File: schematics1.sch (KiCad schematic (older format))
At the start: 14 parts, among them J1 Keypad, SW1 SW_SPST, U1 EA_T123X-I2C

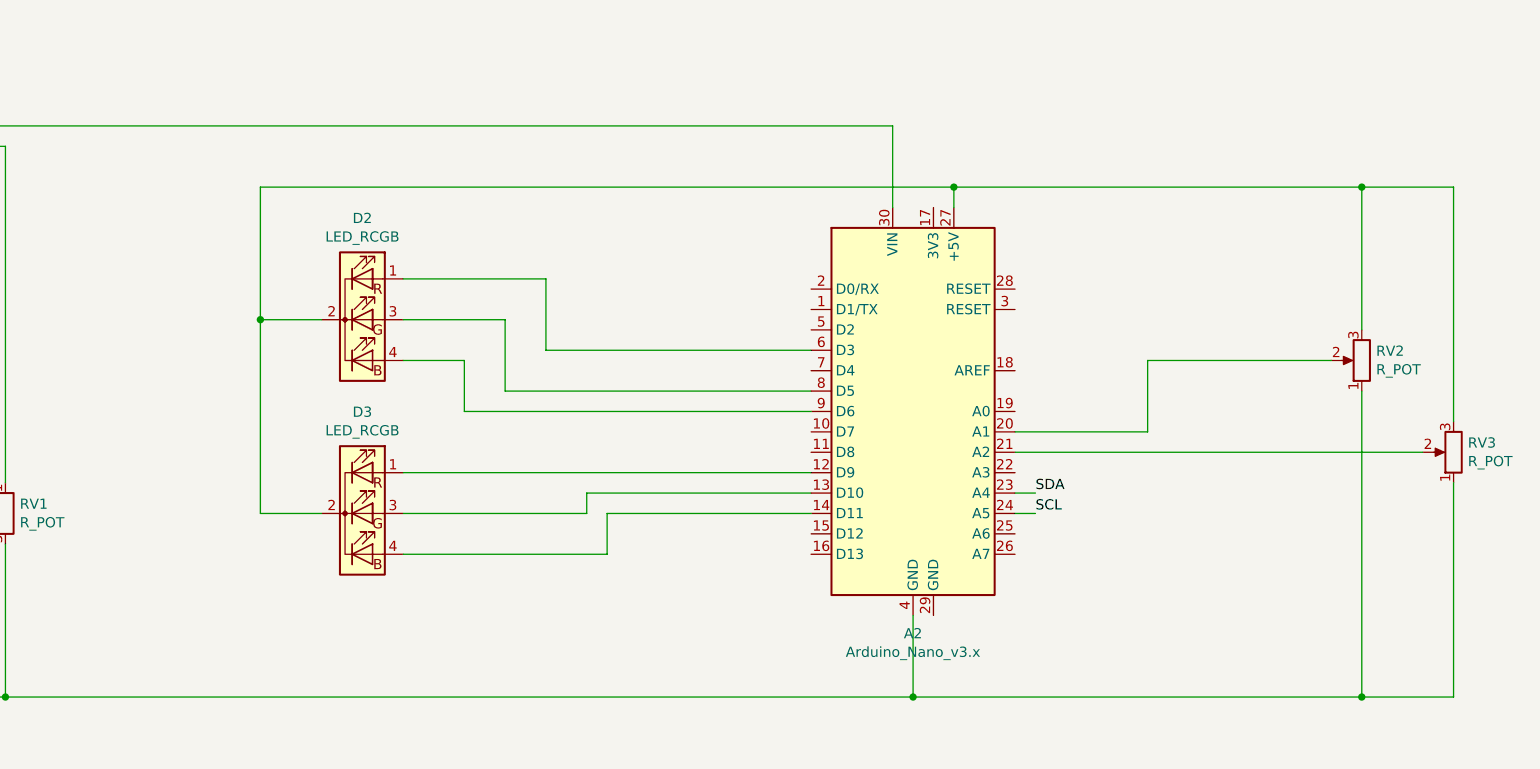
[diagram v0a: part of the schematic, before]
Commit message: Removed RGB, added switches and charlieplex leds to Nano2
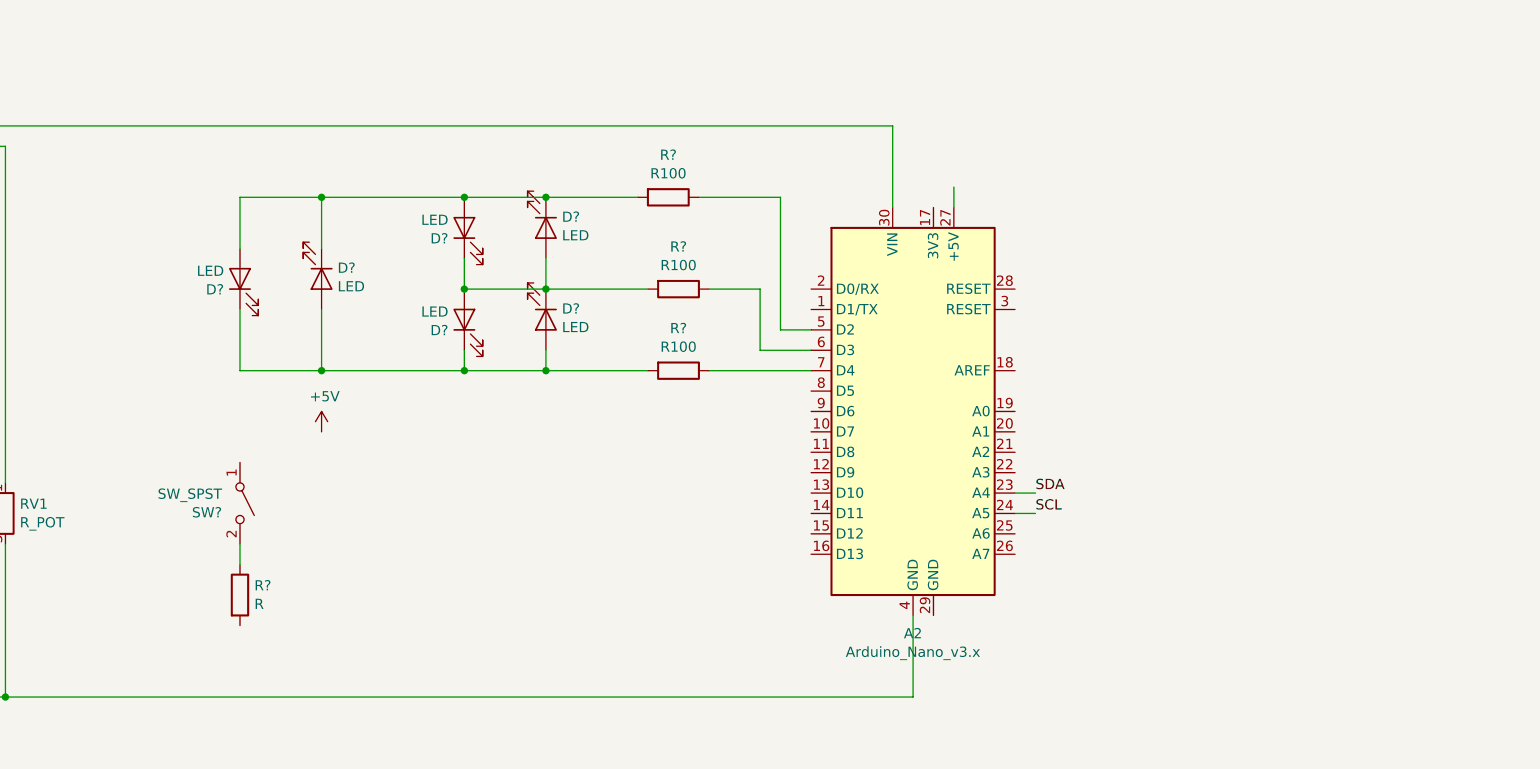
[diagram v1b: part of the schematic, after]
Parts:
- removed D2, D3: LED_RCGB, symbol Device:LED_RCGB
- removed RV2, RV3: R_POT, symbol Device:R_POT
- added D? (x6): LED, symbol Device:LED
- added R? (x3): R100, symbol Device:R
- added R?: R, symbol Device:R
- added SW?: SW_SPST, symbol Switch:SW_SPST
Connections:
- net labels added: +5V
- wire segments 93 -> 86
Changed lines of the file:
@@
 Text Label 5600 4700 0    50   ~ 0
 SDA
-$Comp
-L MCU_Module:Arduino_Nano_v3.x A2
-U 1 1 5D9BED68
-P 11600 4400
-F 0 "A2" H 11600 3311 50  0000 C CNN
-F 1 "Arduino_Nano_v3.x" H 11600 3220 50  0000 C CNN
-F 2 "Module:Arduino_Nano" H 11750 3450 50  0001 L CNN
-F 3 "http://www.mouser.com/pdfdocs/Gravitech_Arduino_Nano3_0.pdf" H 11600 3400 50  0001 C CNN
-	1    11600 4400
-	1    0    0    -1
-$EndComp
 Wire Wire Line
 	4900 3000 4900 3300
@@
 	3950 5800 5000 5800
 Connection ~ 5000 5800
-$Comp
-L Device:LED_RCGB D2
-U 1 1 5D9FD82A
-P 8900 3950
-F 0 "D2" H 8900 4447 50  0000 C CNN
-F 1 "LED_RCGB" H 8900 4356 50  0000 C CNN
-F 2 "" H 8900 3900 50  0001 C CNN
-F 3 "~" H 8900 3900 50  0001 C CNN
-	1    8900 3950
-	1    0    0    -1
-$EndComp
-$Comp
-L Device:LED_RCGB D3
-U 1 1 5D9FEB80
-P 8900 4900
-F 0 "D3" H 8900 5397 50  0000 C CNN
-F 1 "LED_RCGB" H 8900 5306 50  0000 C CNN
-F 2 "" H 8900 4850 50  0001 C CNN
-F 3 "~" H 8900 4850 50  0001 C CNN
-	1    8900 4900
-	1    0    0    -1
-$EndComp
-Wire Wire Line
-	9100 3750 9800 3750
-Wire Wire Line
-	9800 3750 9800 4100
-Wire Wire Line
-	9800 4100 11100 4100
-Wire Wire Line
-	9100 3950 9600 3950
-Wire Wire Line
-	9600 3950 9600 4300
-Wire Wire Line
-	9600 4300 11100 4300
-Wire Wire Line
-	9100 4150 9400 4150
-Wire Wire Line
-	9400 4150 9400 4400
-Wire Wire Line
-	9400 4400 11100 4400
-Wire Wire Line
-	11100 4700 9100 4700
-Wire Wire Line
-	9100 4900 10000 4900
-Wire Wire Line
-	10000 4900 10000 4800
-Wire Wire Line
-	10000 4800 11100 4800
-Wire Wire Line
-	11100 4900 10100 4900
-Wire Wire Line
-	10100 4900 10100 5100
-Wire Wire Line
-	10100 5100 9100 5100
 Wire Wire Line
 	6450 3000 11500 3000
@@
 Wire Wire Line
 	11800 3400 11800 3300
-Wire Wire Line
-	11800 3300 8400 3300
-Wire Wire Line
-	8400 3300 8400 3950
-Wire Wire Line
-	8400 4900 8700 4900
-Wire Wire Line
-	8700 3950 8400 3950
-Connection ~ 8400 3950
-Wire Wire Line
-	8400 3950 8400 4900
-$Comp
-L Device:R_POT RV2
-U 1 1 5DA10FB2
-P 13800 4150
-F 0 "RV2" H 13730 4104 50  0000 R CNN
-F 1 "R_POT" H 13730 4195 50  0000 R CNN
-F 2 "" H 13800 4150 50  0001 C CNN
-F 3 "~" H 13800 4150 50  0001 C CNN
-	1    13800 4150
-	-1   0    0    1
-$EndComp
-$Comp
-L Device:R_POT RV3
-U 1 1 5DA12230
-P 14250 4600
-F 0 "RV3" H 14180 4554 50  0000 R CNN
-F 1 "R_POT" H 14180 4645 50  0000 R CNN
-F 2 "" H 14250 4600 50  0001 C CNN
-F 3 "~" H 14250 4600 50  0001 C CNN
-	1    14250 4600
-	-1   0    0    1
-$EndComp
-Wire Wire Line
-	13650 4150 12750 4150
-Wire Wire Line
-	12750 4150 12750 4500
-Wire Wire Line
-	12750 4500 12100 4500
-Wire Wire Line
-	12100 4600 14100 4600
-Wire Wire Line
-	14250 4450 14250 3300
-Wire Wire Line
-	14250 3300 13800 3300
-Connection ~ 11800 3300
-Wire Wire Line
-	13800 4000 13800 3300
-Connection ~ 13800 3300
-Wire Wire Line
-	13800 3300 11800 3300
-Wire Wire Line
-	11600 5800 13800 5800
-Wire Wire Line
-	14250 5800 14250 4750
-Connection ~ 11600 5800
-Wire Wire Line
-	13800 4300 13800 5800
-Connection ~ 13800 5800
-Wire Wire Line
-	13800 5800 14250 5800
+$Comp
+L Device:LED D?
+U 1 1 5DAAD0C9
+P 8300 3750
+F 0 "D?" V 8247 3828 50  0000 L CNN
+F 1 "LED" V 8338 3828 50  0000 L CNN
+F 2 "" H 8300 3750 50  0001 C CNN
+F 3 "~" H 8300 3750 50  0001 C CNN
+	1    8300 3750
+	0    -1   -1   0
+$EndComp
+$Comp
+L Device:LED D?
+U 1 1 5DAAE2DF
+P 9400 3950
+F 0 "D?" V 9347 4028 50  0000 L CNN
+F 1 "LED" V 9438 4028 50  0000 L CNN
+F 2 "" H 9400 3950 50  0001 C CNN
+F 3 "~" H 9400 3950 50  0001 C CNN
+	1    9400 3950
+	0    -1   -1   0
+$EndComp
+$Comp
+L Device:LED D?
+U 1 1 5DAAE59B
+P 9800 3500
+F 0 "D?" V 9747 3578 50  0000 L CNN
+F 1 "LED" V 9838 3578 50  0000 L CNN
+F 2 "" H 9800 3500 50  0001 C CNN
+F 3 "~" H 9800 3500 50  0001 C CNN
+	1    9800 3500
+	0    1    1    0
+$EndComp
+$Comp
+L Device:LED D?
+U 1 1 5DAAFB45
+P 9400 3500
+F 0 "D?" V 9347 3578 50  0000 L CNN
+F 1 "LED" V 9438 3578 50  0000 L CNN
+F 2 "" H 9400 3500 50  0001 C CNN
+F 3 "~" H 9400 3500 50  0001 C CNN
+	1    9400 3500
+	0    -1   -1   0
+$EndComp
+$Comp
+L Device:LED D?
+U 1 1 5DAAFEED
+P 9800 3950
+F 0 "D?" V 9747 4028 50  0000 L CNN
+F 1 "LED" V 9838 4028 50  0000 L CNN
+F 2 "" H 9800 3950 50  0001 C CNN
+F 3 "~" H 9800 3950 50  0001 C CNN
+	1    9800 3950
+	0    1    1    0
+$EndComp
+$Comp
+L Device:LED D?
+U 1 1 5DAB05F7
+P 8700 3750
+F 0 "D?" V 8647 3828 50  0000 L CNN
+F 1 "LED" V 8738 3828 50  0000 L CNN
+F 2 "" H 8700 3750 50  0001 C CNN
+F 3 "~" H 8700 3750 50  0001 C CNN
+	1    8700 3750
+	0    1    1    0
+$EndComp
+$Comp
+L MCU_Module:Arduino_Nano_v3.x A2
+U 1 1 5D9BED68
+P 11600 4400
+F 0 "A2" H 11600 3311 50  0000 C CNN
+F 1 "Arduino_Nano_v3.x" H 11600 3220 50  0000 C CNN
+F 2 "Module:Arduino_Nano" H 11750 3450 50  0001 L CNN
+F 3 "http://www.mouser.com/pdfdocs/Gravitech_Arduino_Nano3_0.pdf" H 11600 3400 50  0001 C CNN
+	1    11600 4400
+	1    0    0    -1
+$EndComp
+$Comp
+L Device:R R?
+U 1 1 5DAD04B2
+P 10400 3350
+F 0 "R?" V 10193 3350 50  0000 C CNN
+F 1 "R100" V 10284 3350 50  0000 C CNN
+F 2 "" V 10330 3350 50  0001 C CNN
+F 3 "~" H 10400 3350 50  0001 C CNN
+	1    10400 3350
+	0    1    1    0
+$EndComp
+$Comp
+L Device:R R?
+U 1 1 5DAD0C01
+P 10450 3800
+F 0 "R?" V 10243 3800 50  0000 C CNN
+F 1 "R100" V 10334 3800 50  0000 C CNN
+F 2 "" V 10380 3800 50  0001 C CNN
+F 3 "~" H 10450 3800 50  0001 C CNN
+	1    10450 3800
+	0    1    1    0
+$EndComp
+$Comp
+L Device:R R?
+U 1 1 5DAD0EB3
+P 10450 4200
+F 0 "R?" V 10243 4200 50  0000 C CNN
+F 1 "R100" V 10334 4200 50  0000 C CNN
+F 2 "" V 10380 4200 50  0001 C CNN
+F 3 "~" H 10450 4200 50  0001 C CNN
+	1    10450 4200
+	0    1    1    0
+$EndComp
+Wire Wire Line
+	11100 4000 10950 4000
+Wire Wire Line
+	10950 4000 10950 3350
+Wire Wire Line
+	10950 3350 10550 3350
+Wire Wire Line
+	10250 3350 9800 3350
+Wire Wire Line
+	9800 3350 9400 3350
+Wire Wire Line
+	8300 3350 8300 3600
+Connection ~ 9800 3350
+Connection ~ 9400 3350
+Wire Wire Line
+	9400 3350 8700 3350
+Wire Wire Line
+	8700 3600 8700 3350
+Connection ~ 8700 3350
+Wire Wire Line
+	8700 3350 8300 3350
+Wire Wire Line
+	11100 4100 10850 4100
+Wire Wire Line
+	10850 4100 10850 3800
+Wire Wire Line
+	10850 3800 10600 3800
+Wire Wire Line
+	10300 3800 9800 3800
+Wire Wire Line
+	9400 3800 9800 3800
+Connection ~ 9800 3800
+Wire Wire Line
+	9800 3650 9800 3800
+Wire Wire Line
+	9400 3650 9400 3800
+Connection ~ 9400 3800
+Wire Wire Line
+	11100 4200 10600 4200
+Wire Wire Line
+	10300 4200 9800 4200
+Wire Wire Line
+	8300 4200 8300 3900
+Wire Wire Line
+	8700 3900 8700 4200
+Connection ~ 8700 4200
+Wire Wire Line
+	8700 4200 8300 4200
+Wire Wire Line
+	9400 4100 9400 4200
+Connection ~ 9400 4200
+Wire Wire Line
+	9400 4200 8700 4200
+Wire Wire Line
+	9800 4100 9800 4200
+Connection ~ 9800 4200
+Wire Wire Line
+	9800 4200 9400 4200
+$Comp
+L Switch:SW_SPST SW?
+U 1 1 5DAE8628
+P 8300 4850
+F 0 "SW?" V 8346 4762 50  0000 R CNN
+F 1 "SW_SPST" V 8255 4762 50  0000 R CNN
+F 2 "" H 8300 4850 50  0001 C CNN
+F 3 "~" H 8300 4850 50  0001 C CNN
+	1    8300 4850
+	0    1    1    0
+$EndComp
+$Comp
+L Device:R R?
+U 1 1 5DAEDDF2
+P 8300 5300
+F 0 "R?" H 8370 5346 50  0000 L CNN
+F 1 "R" H 8370 5255 50  0000 L CNN
+F 2 "" V 8230 5300 50  0001 C CNN
+F 3 "~" H 8300 5300 50  0001 C CNN
+	1    8300 5300
+	1    0    0    -1
+$EndComp
+Wire Wire Line
+	8300 5050 8300 5150
+$Comp
+L power:+5V #PWR?
+U 1 1 5DAF87E0
+P 8700 4500
+F 0 "#PWR?" H 8700 4350 50  0001 C CNN
+F 1 "+5V" H 8715 4673 50  0000 C CNN
+F 2 "" H 8700 4500 50  0001 C CNN
+F 3 "" H 8700 4500 50  0001 C CNN
+	1    8700 4500
+	1    0    0    -1
+$EndComp
 $EndSCHEMATC

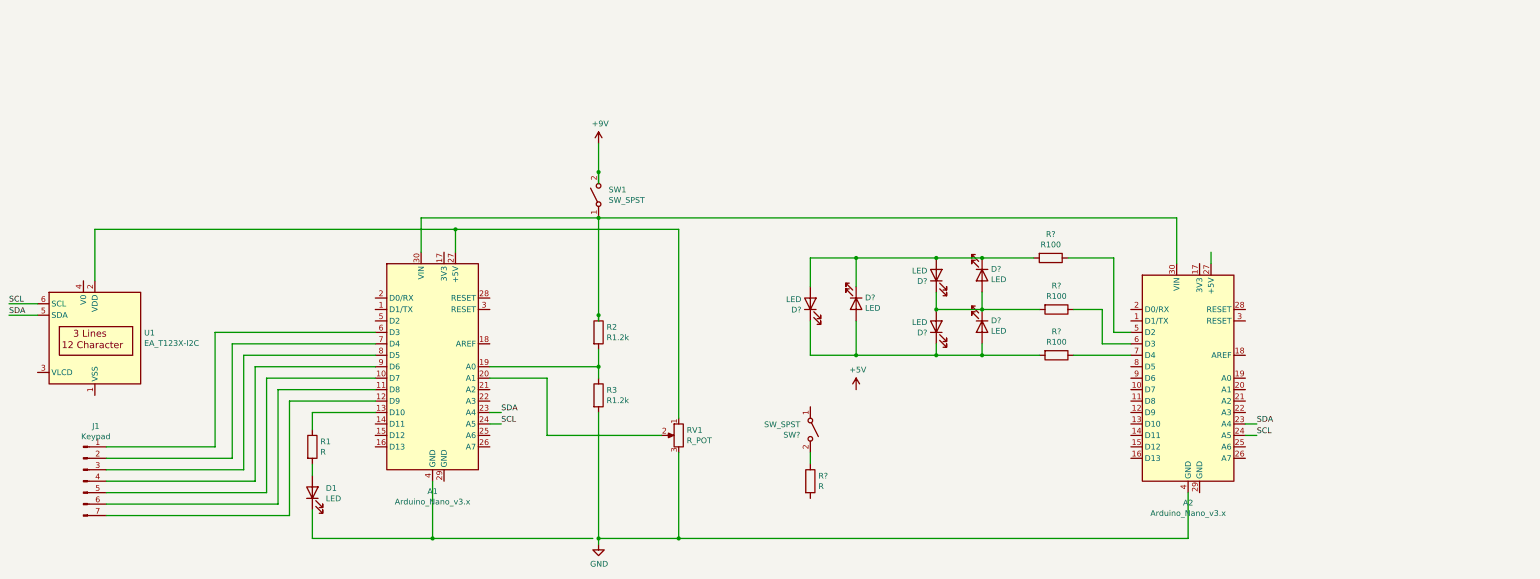
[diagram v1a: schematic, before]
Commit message: Added charlieplexed leds
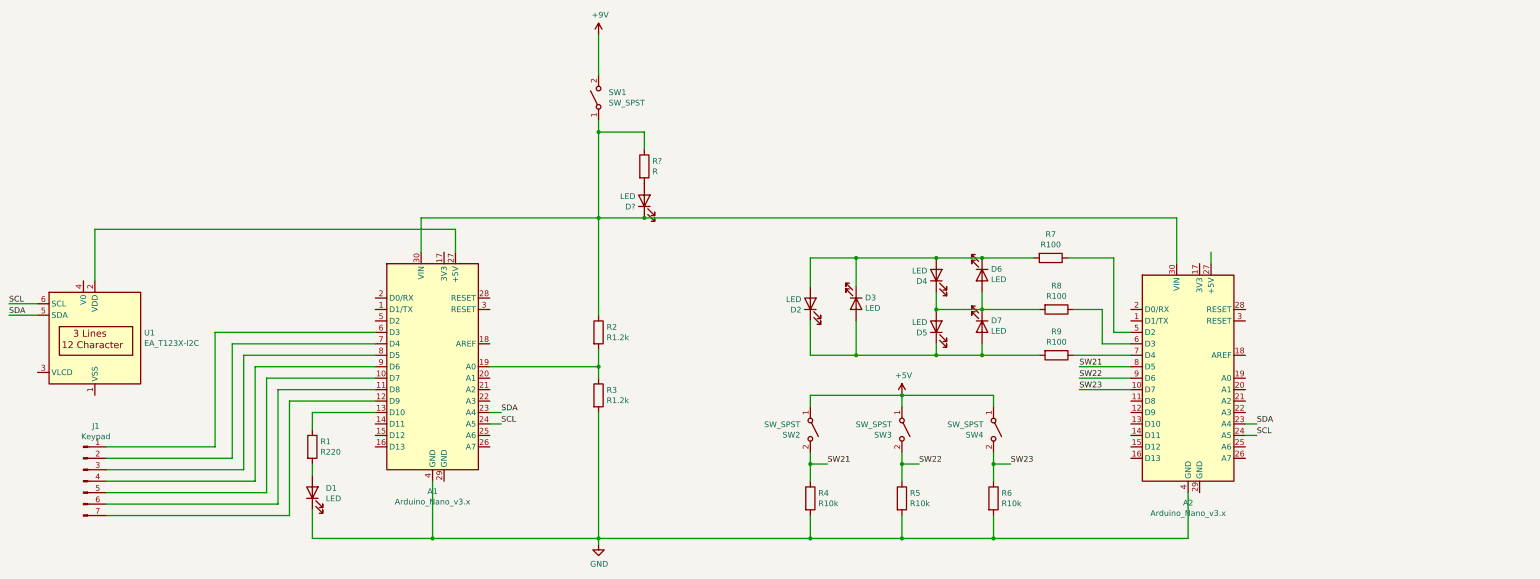
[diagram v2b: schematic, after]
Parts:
- removed RV1: R_POT, symbol Device:R_POT
- added D?: LED, symbol Device:LED
- added R5, R6: R10k, symbol Device:R
- added R?: R, symbol Device:R
- added SW3, SW4: SW_SPST, symbol Switch:SW_SPST
- R1: value R -> R220
- R4: renamed from R?; value R -> R10k
- gave numbers to parts that had none: 10
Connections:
- net labels added: SW21, SW22, SW23
- wire segments 86 -> 104
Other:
- moved on the sheet: R4, SW1
